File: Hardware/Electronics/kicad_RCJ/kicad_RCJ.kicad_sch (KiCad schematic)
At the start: 79 parts, among them J1 Raspberry_Pi_2_3, J10 Conn_01x04_M1_extra, J11 Conn_01x04_M2_extra, J12 Conn_01x04_M3_extra, J13 Conn_01x04_M4_extra, J14 Conn_01x06_teensy_left_extra, J15 Conn_01x04_teensy_right_extra, J16 Conn_01x07_IO_expander_extra, J17 Conn_02x03_I2C, J18 Conn_02x05_3V3_GND, J19 Conn_02x05_5V_GND, J2 Conn_01x06_IMU_extra, J20 Conn_01x06_BNO085_extra, J21 Conn_01x06_ISM20948_extra, J22 Conn_01x02_LSM5DSOX_LIS3MDL_e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, J3 Conn_01x02_colsens_interrupt, J4 Conn_01x02_5V, J5 Conn_01x02_3V3, J6 Conn_01x02_I2C1, J7 Conn_01x01_LOP, J8 Conn_01x03_IO_expander_interr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, J9 Conn_01x06_LED, M5 Servo1, M6 Servo2, U12 VL53L0/1X, U13 VL53L0/1X, U14 VL53L0/1X, U15 VL53L0/1X, U16 VL53L0/1X, U17 VL53L0/1X, U18 VL53L0/1X, U20 BNO085, U21 ICM20948, U22 LSM6DSOX+LIS3MDL, U23 TCS34725, U24 APDS9960, U25 VL53L0/1X

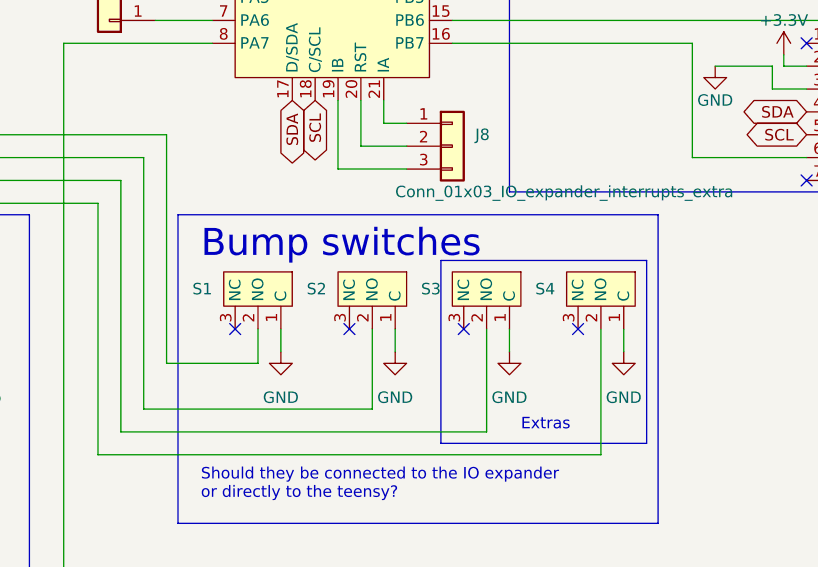
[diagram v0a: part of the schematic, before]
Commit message: added some footprints and began laying out pcb
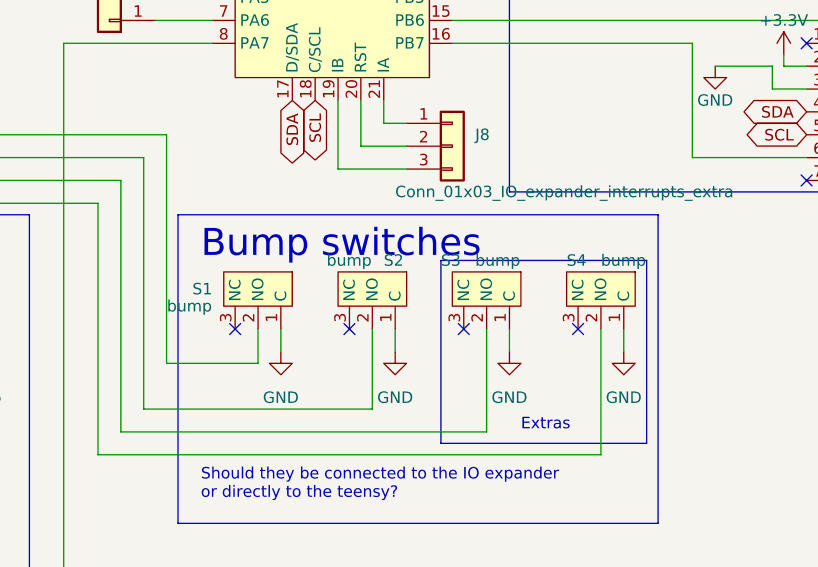
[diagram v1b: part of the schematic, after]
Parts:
- D3, D4, D5, D6, D7, D8: footprint (none) -> Connector_PinSocket_2.54mm:PinSocket_1x03_P2.54mm_Vertical
- J17: footprint (none) -> Connector_PinSocket_2.54mm:PinSocket_2x03_P2.54mm_Vertical
- J18, J19: footprint (none) -> Connector_PinSocket_2.54mm:PinSocket_2x05_P2.54mm_Vertical
- J20, J21: footprint (none) -> Connector_PinSocket_2.54mm:PinSocket_1x06_P2.54mm_Vertical
- J22: footprint (none) -> Connector_PinSocket_2.54mm:PinSocket_1x02_P2.54mm_Vertical
- J8: footprint Connector_JST:JST_XH_B3B-XH-A_1x03_P2.50mm_Vertical -> Connector_PinSocket_2.54mm:PinSocket_1x03_P2.54mm_Vertical
- R11, R5, R7, R9: footprint (none) -> Connector_JST:JST_XH_B2B-XH-A_1x02_P2.50mm_Vertical
- S1, S2, S3, S4: value ~ -> bump; footprint (none) -> Connector_JST:JST_XH_B3B-XH-A_1x03_P2.50mm_Vertical
- U23: footprint (none) -> Connector_JST:JST_XH_B6B-XH-A_1x06_P2.50mm_Vertical
- U24: footprint (none) -> Connector_JST:JST_XH_B5B-XH-A_1x05_P2.50mm_Vertical
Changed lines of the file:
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@@
       (effects (font (size 1.27 1.27)))
     )
-    (property "Footprint" "" (at 161.29 217.17 0)
+    (property "Footprint" "Connector_PinSocket_2.54mm:PinSocket_1x03_P2.54mm_Vertical" (at 161.29 217.17 0)
       (effects (font (size 1.27 1.27)) hide)
     )
@@
   )
   (symbol (lib_id "RCJ_parts:SW_limit") (at 325.12 111.76 0) (mirror y) (unit 1)
-    (in_bom yes) (on_board yes) (dnp no) (fields_autoplaced)
-    (property "Reference" "S3" (at 317.5 114.935 0)
-      (effects (font (size 1.27 1.27)) (justify left))
+    (in_bom yes) (on_board yes) (dnp no)
+    (property "Reference" "S3" (at 317.5 111.76 0)
+      (effects (font (size 1.27 1.27)) (justify right))
     )
-    (property "Value" "~" (at 325.12 111.76 0)
-      (effects (font (size 1.27 1.27)))
+    (property "Value" "bump" (at 321.31 111.76 0)
+      (effects (font (size 1.27 1.27)) (justify right))
     )
-    (property "Footprint" "" (at 325.12 111.76 0)
+    (property "Footprint" "Connector_JST:JST_XH_B3B-XH-A_1x03_P2.50mm_Vertical" (at 325.12 111.76 0)
       (effects (font (size 1.27 1.27)) hide)
     )
@@
       (effects (font (size 1.27 1.27)))
     )
-    (property "Footprint" "" (at 129.54 212.09 0)
+    (property "Footprint" "Connector_PinSocket_2.54mm:PinSocket_1x03_P2.54mm_Vertical" (at 129.54 212.09 0)
       (effects (font (size 1.27 1.27)) hide)
     )
@@
   )
   (symbol (lib_id "RCJ_parts:SW_limit") (at 299.72 111.76 0) (mirror y) (unit 1)
-    (in_bom yes) (on_board yes) (dnp no) (fields_autoplaced)
+    (in_bom yes) (on_board yes) (dnp no)
     (property "Reference" "S1" (at 292.1 114.935 0)
       (effects (font (size 1.27 1.27)) (justify left))
     )
-    (property "Value" "~" (at 299.72 111.76 0)
+    (property "Value" "bump" (at 289.56 116.84 0)
       (effects (font (size 1.27 1.27)))
     )
-    (property "Footprint" "" (at 299.72 111.76 0)
+    (property "Footprint" "Connector_JST:JST_XH_B3B-XH-A_1x03_P2.50mm_Vertical" (at 299.72 111.76 0)
       (effects (font (size 1.27 1.27)) hide)
     )
@@
       (effects (font (size 1.27 1.27)))
     )
-    (property "Footprint" "" (at 160.02 149.86 0)
+    (property "Footprint" "Connector_PinSocket_2.54mm:PinSocket_1x06_P2.54mm_Vertical" (at 160.02 149.86 0)
       (effects (font (size 1.27 1.27)) hide)
     )
@@
       (effects (font (size 1.27 1.27)))
     )
-    (property "Footprint" "" (at 194.31 132.08 0)
+    (property "Footprint" "Connector_PinSocket_2.54mm:PinSocket_2x05_P2.54mm_Vertical" (at 194.31 132.08 0)
       (effects (font (size 1.27 1.27)) hide)
     )
@@
       (effects (font (size 1.27 1.27)))
     )
-    (property "Footprint" "" (at 146.05 223.52 0)
+    (property "Footprint" "Connector_PinSocket_2.54mm:PinSocket_1x03_P2.54mm_Vertical" (at 146.05 223.52 0)
       (effects (font (size 1.27 1.27)) hide)
     )
@@
       (effects (font (size 1.27 1.27)))
     )
-    (property "Footprint" "" (at 225.425 154.94 0)
+    (property "Footprint" "Connector_JST:JST_XH_B6B-XH-A_1x06_P2.50mm_Vertical" (at 225.425 154.94 0)
       (effects (font (size 1.27 1.27)) hide)
     )
@@
       (effects (font (size 1.27 1.27)))
     )
-    (property "Footprint" "" (at 129.54 223.52 0)
+    (property "Footprint" "Connector_PinSocket_2.54mm:PinSocket_1x03_P2.54mm_Vertical" (at 129.54 223.52 0)
       (effects (font (size 1.27 1.27)) hide)
     )
@@
       (effects (font (size 1.27 1.27)) (justify left))
     )
-    (property "Footprint" "" (at 260.35 132.08 90)
+    (property "Footprint" "Connector_JST:JST_XH_B2B-XH-A_1x02_P2.50mm_Vertical" (at 260.35 132.08 90)
       (effects (font (size 1.27 1.27)) (justify left) hide)
     )
@@
       (effects (font (size 1.27 1.27)))
     )
-    (property "Footprint" "" (at 203.2 24.13 0)
+    (property "Footprint" "Connector_PinSocket_2.54mm:PinSocket_2x03_P2.54mm_Vertical" (at 203.2 24.13 0)
       (effects (font (size 1.27 1.27)) hide)
     )
@@
   )
   (symbol (lib_id "RCJ_parts:SW_limit") (at 337.82 111.76 0) (mirror y) (unit 1)
-    (in_bom yes) (on_board yes) (dnp no) (fields_autoplaced)
-    (property "Reference" "S4" (at 330.2 114.935 0)
-      (effects (font (size 1.27 1.27)) (justify left))
+    (in_bom yes) (on_board yes) (dnp no)
+    (property "Reference" "S4" (at 331.47 111.76 0)
+      (effects (font (size 1.27 1.27)) (justify right))
     )
-    (property "Value" "~" (at 337.82 111.76 0)
-      (effects (font (size 1.27 1.27)))
+    (property "Value" "bump" (at 335.28 111.76 0)
+      (effects (font (size 1.27 1.27)) (justify right))
     )
-    (property "Footprint" "" (at 337.82 111.76 0)
+    (property "Footprint" "Connector_JST:JST_XH_B3B-XH-A_1x03_P2.50mm_Vertical" (at 337.82 111.76 0)
       (effects (font (size 1.27 1.27)) hide)
     )
@@
       (effects (font (size 1.27 1.27)))
     )
-    (property "Footprint" "" (at 254 154.94 0)
+    (property "Footprint" "Connector_JST:JST_XH_B5B-XH-A_1x05_P2.50mm_Vertical" (at 254 154.94 0)
       (effects (font (size 1.27 1.27)) hide)
     )
@@
       (effects (font (size 1.27 1.27)) (justify left))
     )
-    (property "Footprint" "" (at 246.38 132.08 90)
+    (property "Footprint" "Connector_JST:JST_XH_B2B-XH-A_1x02_P2.50mm_Vertical" (at 246.38 132.08 90)
       (effects (font (size 1.27 1.27)) (justify left) hide)
     )
@@
       (effects (font (size 1.27 1.27)) (justify left))
     )
-    (property "Footprint" "Connector_JST:JST_XH_B3B-XH-A_1x03_P2.50mm_Vertical" (at 318.77 99.06 0)
+    (property "Footprint" "Connector_PinSocket_2.54mm:PinSocket_1x03_P2.54mm_Vertical" (at 318.77 99.06 0)
       (effects (font (size 1.27 1.27)) hide)
     )
@@
       (effects (font (size 1.27 1.27)))
     )
-    (property "Footprint" "" (at 161.29 205.74 0)
+    (property "Footprint" "Connector_PinSocket_2.54mm:PinSocket_1x03_P2.54mm_Vertical" (at 161.29 205.74 0)
       (effects (font (size 1.27 1.27)) hide)
     )
@@
       (effects (font (size 1.27 1.27)))
     )
-    (property "Footprint" "" (at 137.16 149.86 0)
+    (property "Footprint" "Connector_PinSocket_2.54mm:PinSocket_1x06_P2.54mm_Vertical" (at 137.16 149.86 0)
       (effects (font (size 1.27 1.27)) hide)
     )
@@
       (effects (font (size 1.27 1.27)) (justify left))
     )
-    (property "Footprint" "" (at 219.71 132.08 90)
+    (property "Footprint" "Connector_JST:JST_XH_B2B-XH-A_1x02_P2.50mm_Vertical" (at 219.71 132.08 90)
       (effects (font (size 1.27 1.27)) (justify left) hide)
     )
@@
       (effects (font (size 1.27 1.27)))
     )
-    (property "Footprint" "" (at 146.05 212.09 0)
+    (property "Footprint" "Connector_PinSocket_2.54mm:PinSocket_1x03_P2.54mm_Vertical" (at 146.05 212.09 0)
       (effects (font (size 1.27 1.27)) hide)
     )
@@
       (effects (font (size 1.27 1.27)) (justify left))
     )
-    (property "Footprint" "" (at 232.41 132.08 90)
+    (property "Footprint" "Connector_JST:JST_XH_B2B-XH-A_1x02_P2.50mm_Vertical" (at 232.41 132.08 90)
       (effects (font (size 1.27 1.27)) (justify left) hide)
     )
@@
       (effects (font (size 1.27 1.27)) (justify right))
     )
-    (property "Footprint" "" (at 177.8 149.86 0)
+    (property "Footprint" "Connector_PinSocket_2.54mm:PinSocket_1x02_P2.54mm_Vertical" (at 177.8 149.86 0)
       (effects (font (size 1.27 1.27)) hide)
     )
@@
       (effects (font (size 1.27 1.27)))
     )
-    (property "Footprint" "" (at 241.3 27.94 0)
+    (property "Footprint" "Connector_PinSocket_2.54mm:PinSocket_2x05_P2.54mm_Vertical" (at 241.3 27.94 0)
       (effects (font (size 1.27 1.27)) hide)
     )
@@
   )
   (symbol (lib_id "RCJ_parts:SW_limit") (at 312.42 111.76 0) (mirror y) (unit 1)
-    (in_bom yes) (on_board yes) (dnp no) (fields_autoplaced)
-    (property "Reference" "S2" (at 304.8 114.935 0)
-      (effects (font (size 1.27 1.27)) (justify left))
+    (in_bom yes) (on_board yes) (dnp no)
+    (property "Reference" "S2" (at 311.15 111.76 0)
+      (effects (font (size 1.27 1.27)) (justify right))
     )
-    (property "Value" "~" (at 312.42 111.76 0)
-      (effects (font (size 1.27 1.27)))
+    (property "Value" "bump" (at 304.8 111.76 0)
+      (effects (font (size 1.27 1.27)) (justify right))
     )
-    (property "Footprint" "" (at 312.42 111.76 0)
+    (property "Footprint" "Connector_JST:JST_XH_B3B-XH-A_1x03_P2.50mm_Vertical" (at 312.42 111.76 0)
       (effects (font (size 1.27 1.27)) hide)
     )

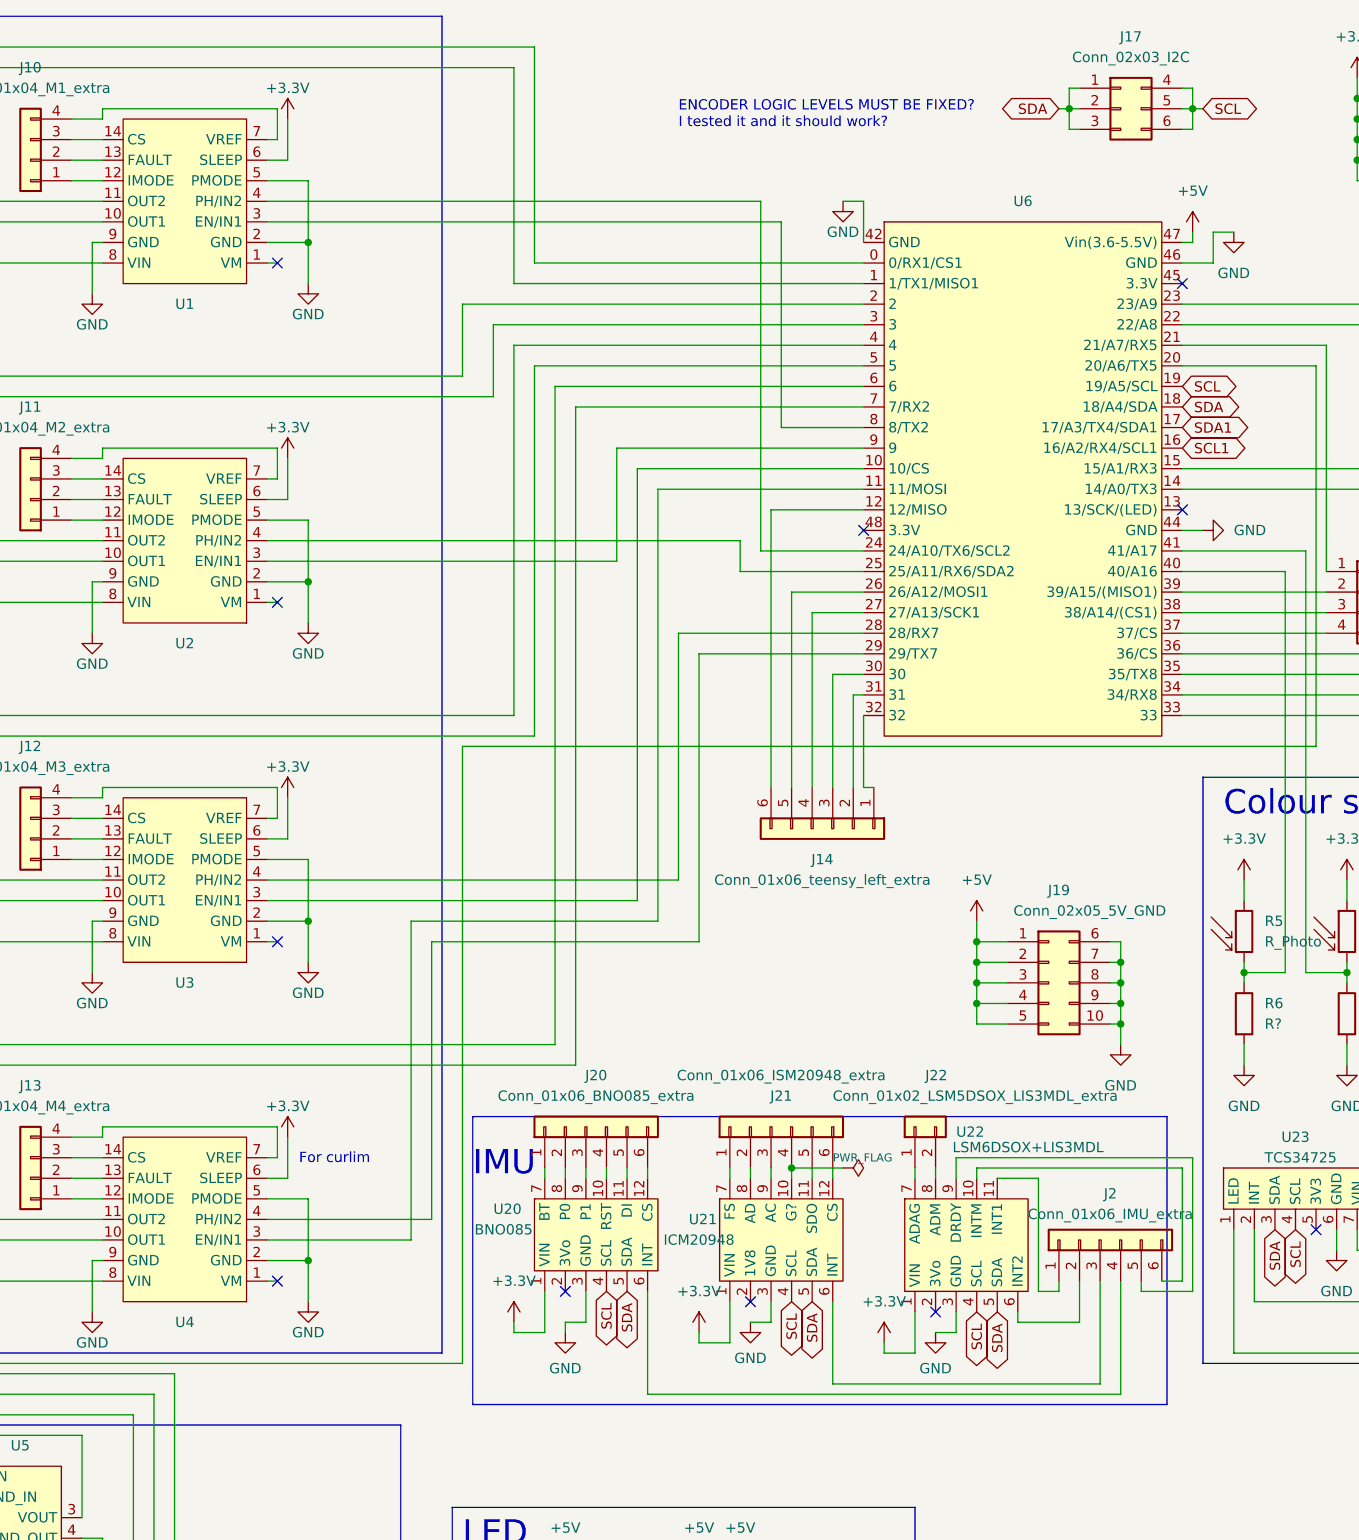
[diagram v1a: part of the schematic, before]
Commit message: added some footprints and did some PCB layout work
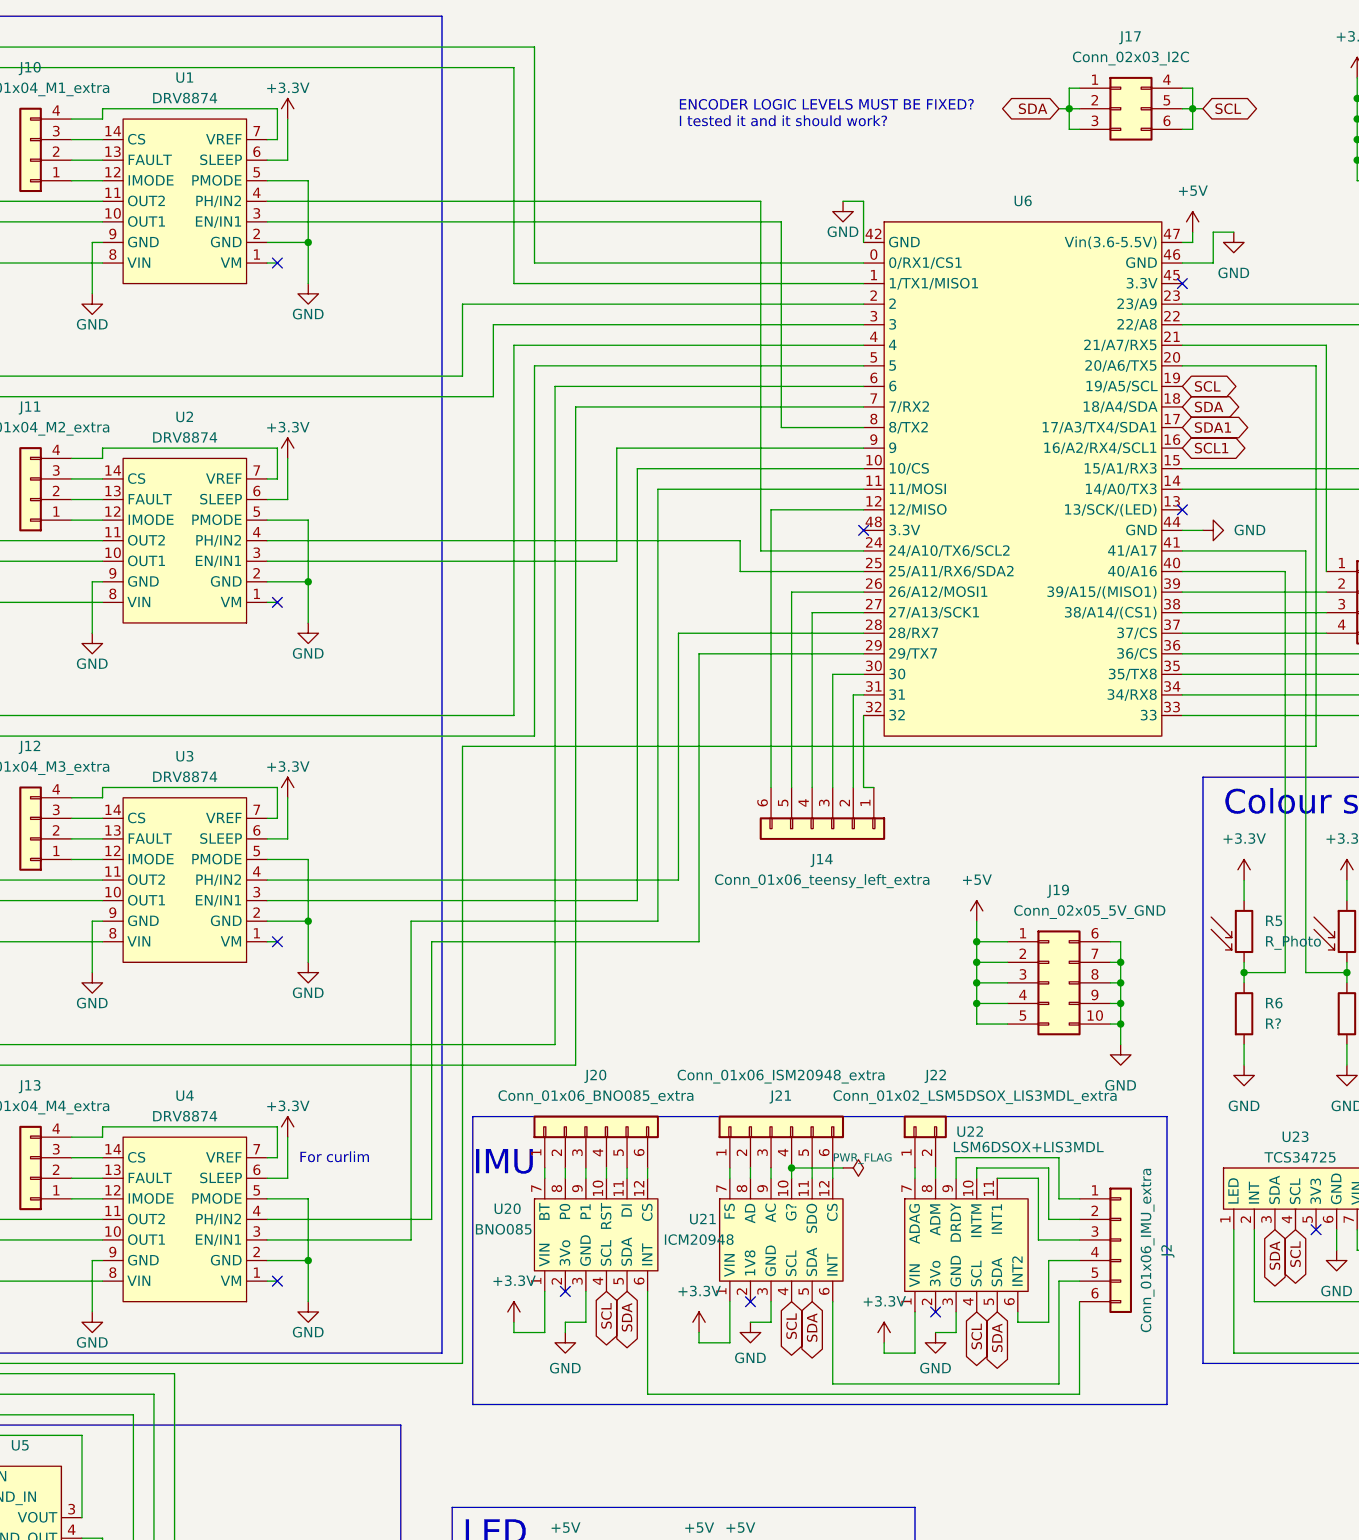
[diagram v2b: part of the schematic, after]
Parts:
- U1, U2, U3, U4: value ~ -> DRV8874; footprint (none) -> RCJ2024_kicad_footprints:DRV8874
- U20: footprint (none) -> RCJ2024_kicad_footprints:BNO085
- U21: footprint (none) -> RCJ2024_kicad_footprints:ICM2049
- U22: footprint (none) -> RCJ2024_kicad_footprints:LSM6DSOX+LIS3MDL
- U6: footprint (none) -> RCJ2024_kicad_footprints:Teensy_41
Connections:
- net at U21.6 (INT): now also J2.5 (Pin_5); no longer J2.3 (Pin_3)
- net at U22.10 (INTM): now also J2.2 (Pin_2); no longer J2.6 (Pin_6)
- net at U22.11 (INT1): now also J2.3 (Pin_3); no longer J2.1 (Pin_1)
- net at U22.6 (INT2): now also J2.4 (Pin_4); no longer J2.2 (Pin_2)
- net at U22.9 (DRDY): now also J2.1 (Pin_1); no longer J2.5 (Pin_5)
- net at U20.6 (INT): now also J2.6 (Pin_6); no longer J2.4 (Pin_4)
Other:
- moved on the sheet: J2

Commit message: worked on PCB layout, made footprints etc.
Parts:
- U19: footprint (none) -> RCJ2024_kicad_footprints:IO_Expander
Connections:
- net +3.3V: now also U19.23 (VCC); no longer U19. (VCC)
- net GND: now also U19.22 (GND); no longer U19. (VCC)
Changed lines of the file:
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@@
   (symbol (lib_id "RCJ_parts:DFRobot_IO_expander") (at 294.64 63.5 0) (unit 1)
     (in_bom yes) (on_board yes) (dnp no) (fields_autoplaced)
-    (property "Reference" "U19" (at 320.675 65.4619 0)
-      (effects (font (size 1.27 1.27)))
+    (property "Reference" "U19" (at 313.3441 63.5 0)
+      (effects (font (size 1.27 1.27)) (justify left))
     )
     (property "Value" "~" (at 279.4 63.5 0)
       (effects (font (size 1.27 1.27)))
     )
-    (property "Footprint" "" (at 279.4 63.5 0)
+    (property "Footprint" "RCJ2024_kicad_footprints:IO_Expander" (at 279.4 63.5 0)
       (effects (font (size 1.27 1.27)) hide)
     )
@@
       (effects (font (size 1.27 1.27)) hide)
     )
-    (pin "")
-    (pin "")
+    (pin "25")
+    (pin "23")
     (pin "1")
     (pin "10")
@@
     (pin "8")
     (pin "9")
-    (pin "")
-    (pin "")
+    (pin "22")
+    (pin "24")
     (instances
       (project "kicad_RCJ"
